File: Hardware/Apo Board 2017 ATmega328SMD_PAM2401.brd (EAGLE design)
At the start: 85.1 x 52.7 mm, 41 parts, among them Q1 RESONATORSMD, U1 PAM2401, U13 ATMEGA328

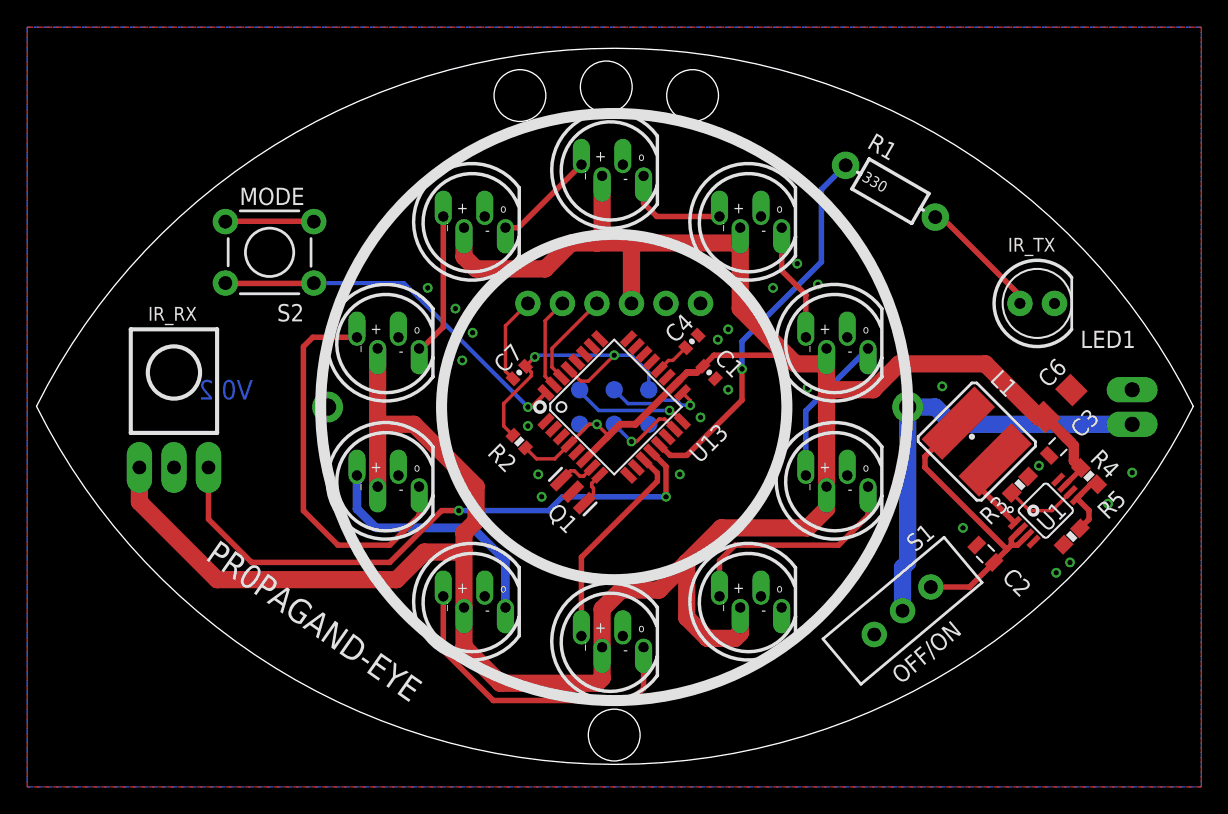
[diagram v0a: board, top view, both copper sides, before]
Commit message: Updating Battery footprint
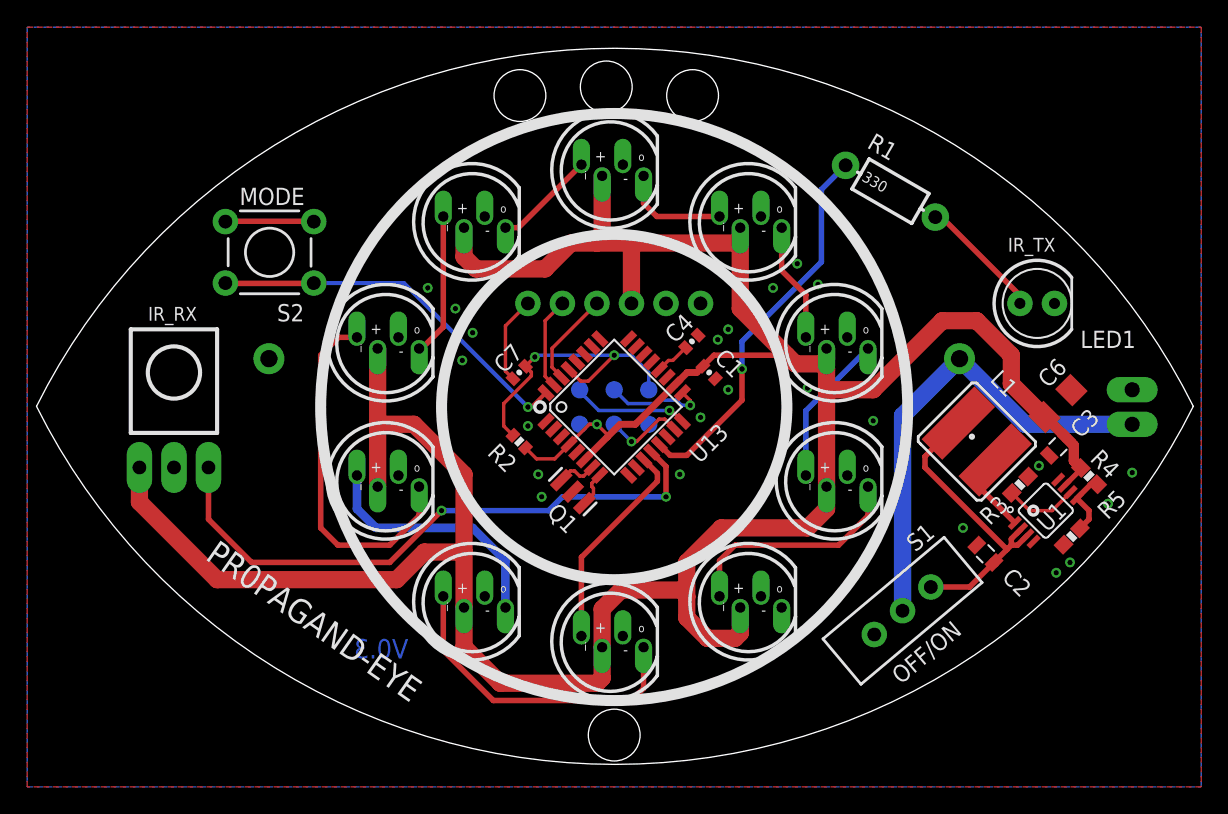
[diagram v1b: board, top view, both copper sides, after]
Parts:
- U10, U11, U2, U3, U4, U5, U6, U7, U8, U9: value (none) -> LED-TRICOLOR-5050-ICWS2812-THRU-KIT
- moved LOGO1 48.3 mm to (15.3, -17.7)
- moved BATT1 4.02 mm to (0.00, 3.81)
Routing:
- net +BATT_RAW: track 32.2 -> 35.0 mm
- net +5V: track 219.1 -> 221.6 mm
- net N$5: track 28.9 -> 26.7 mm
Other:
- board text added: "V0.3"
- board text removed: "V0.2"
